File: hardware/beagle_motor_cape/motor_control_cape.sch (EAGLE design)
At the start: 26 parts, among them IC1 MCP4911SN, IC2 MCP4911SN

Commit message: Continue work on BeagleBone Black cape
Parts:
- removed IC3: (no value), INA219:INA219-SO8D
- added C4, C5, C6: 0.1uF, resistor:C-USC0603
- added D1, D2, D3, D4: 3.3V, diode:ZENER-DIODESOT23
- added LED1, LED2: (no value), adafruit:LEDCHIPLED_0603
- added Q7, Q8: (no value), adafruit:MOSFET-NREFLOW
- added R14, R15: 1k, rcl:R-US_R0603
- added R16, R18: 2k, rcl:R-US_R0603
- added R17: 11.3k, rcl:R-US_R0603
- added U1, U2: BTS50055-1TMA, BTS50055-1TMA:BTS50055-1TMA
- C3: value 1uF -> 0.1uF
- R10: value DNP -> 0
- R11: value DNP -> 681
- R12: value 4.7k -> 1k
- R13: value 4.7k -> 11.3k
- R7: value CSS2H-2512R-1L00F -> 681; device resistor:R-US_R6332 -> rcl:R-US_R0603
- R8: value 1k -> 0
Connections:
- net MOTOR0_SENSE renamed MOTOR0_TACH
- net MOTOR1_SENSE renamed MOTOR1_TACH
- removed net BATT0_IN: IC3.VIN+, R7.2
- removed net BATT0_OUT: IC3.VIN-, R7.1
- removed net I2C_SCL: IC3.SCL, R13.1
- removed net I2C_SDA: IC3.SDA, R12.1
- new net MOTOR0_EN: Q7.G, R14.2, R15.2
- new net MOTOR0_SENSE_AD: R10.2
- new net MOTOR1_EN: Q8.G, R12.2, R9.2
- new net MOTOR1_SENSE_AD: R8.2
- new net N$4: C4.1, D1.C, R10.1, R11.2, U1.IS
- new net N$5: Q7.D, U1.IN
- new net N$6: LED1.A, R15.1
- new net VCC: R13.2, U1.VBB@1, U1.VBB@2
- new net VCC_SENSE_AD: C5.1, D3.C, R13.1, R16.1
- new net VDD: R17.2, U2.VBB@1, U2.VBB@2
- new net VDD_SENSE_AD: C6.1, D4.C, R17.1, R18.1
- net +3V3: no longer R12.2, R13.2, R8.2, R9.2
- net GND: now also C4.2, C5.2, C6.2, D1.A, D2.A, D3.A, D4.A, LED1.C, LED2.C, Q7.S, Q8.S, R14.1, R16.2, R18.2, R7.1, R9.1, U1.OUT1, U1.OUT2, U1.OUT3, U1.OUT4, U2.OUT1, U2.OUT2, U2.OUT3, U2.OUT4; no longer R10.1
- net N$1: now also C3.1, D2.C, R7.2, R8.1, U2.IS; no longer IC3.A1, R10.2, R9.1
- net N$2: now also Q8.D, U2.IN; no longer IC3.A0, R11.2, R8.1
- net N$3: now also LED2.A, R12.1; no longer C3.1
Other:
- note added: "/FWD"
- note added: "/LDAC"
- note added: "/REV"
- note added: "1. Beaglebone Connector 2. Power Supply 3. Connectors 4. DAC and GPIO 5. High Side Switches"
- note added: "20V"
- note added: "3.3V Analog"
- note added: "ANA_X"
- note added: "BATT+"
- note added: "BATT-"
- note added: "BEAGLEBONE"
- note added: "CS"
- note added: "Connectors"
- note added: "DAC"
- note added: "ENABLE"
- note added: "FWD"
- note added: "GND"
- note added: "GPIO"
- note added: "GPIO_X"
- note added: "HS-Switch"
- note added: "High Side Switches"
- note added: "MOSI"
- note added: "MOTOR 0"
- note added: "MOTOR 1"
- note added: "OUT"
- note added: "PWM"
- note added: "Power Supply"
- note added: "REV"
- note added: "Ris sized to produce ~3V when IL = 60A"
- note added: "SCLK"
- note added: "SENSE"
- note added: "SPI0"
- note added: "SPI1"
- note added: "TACH"
- note added: "TRIGGER"
- note added: "VCC"
- note added: "VCC at 20V produces 3V on VCC_SENSE"
- note added: "VCC, VDD are independently supplied by one 1 battery pack each ~20V fully charged"
- note added: "VDD at 20V produces 3V on VDD_SENSE"
- note removed: "1. Beaglebone Connector 2. Power Suppply 3. DAC and GPIO"
- note removed: "Beaglebone Connector"
- note removed: "Current Sense"

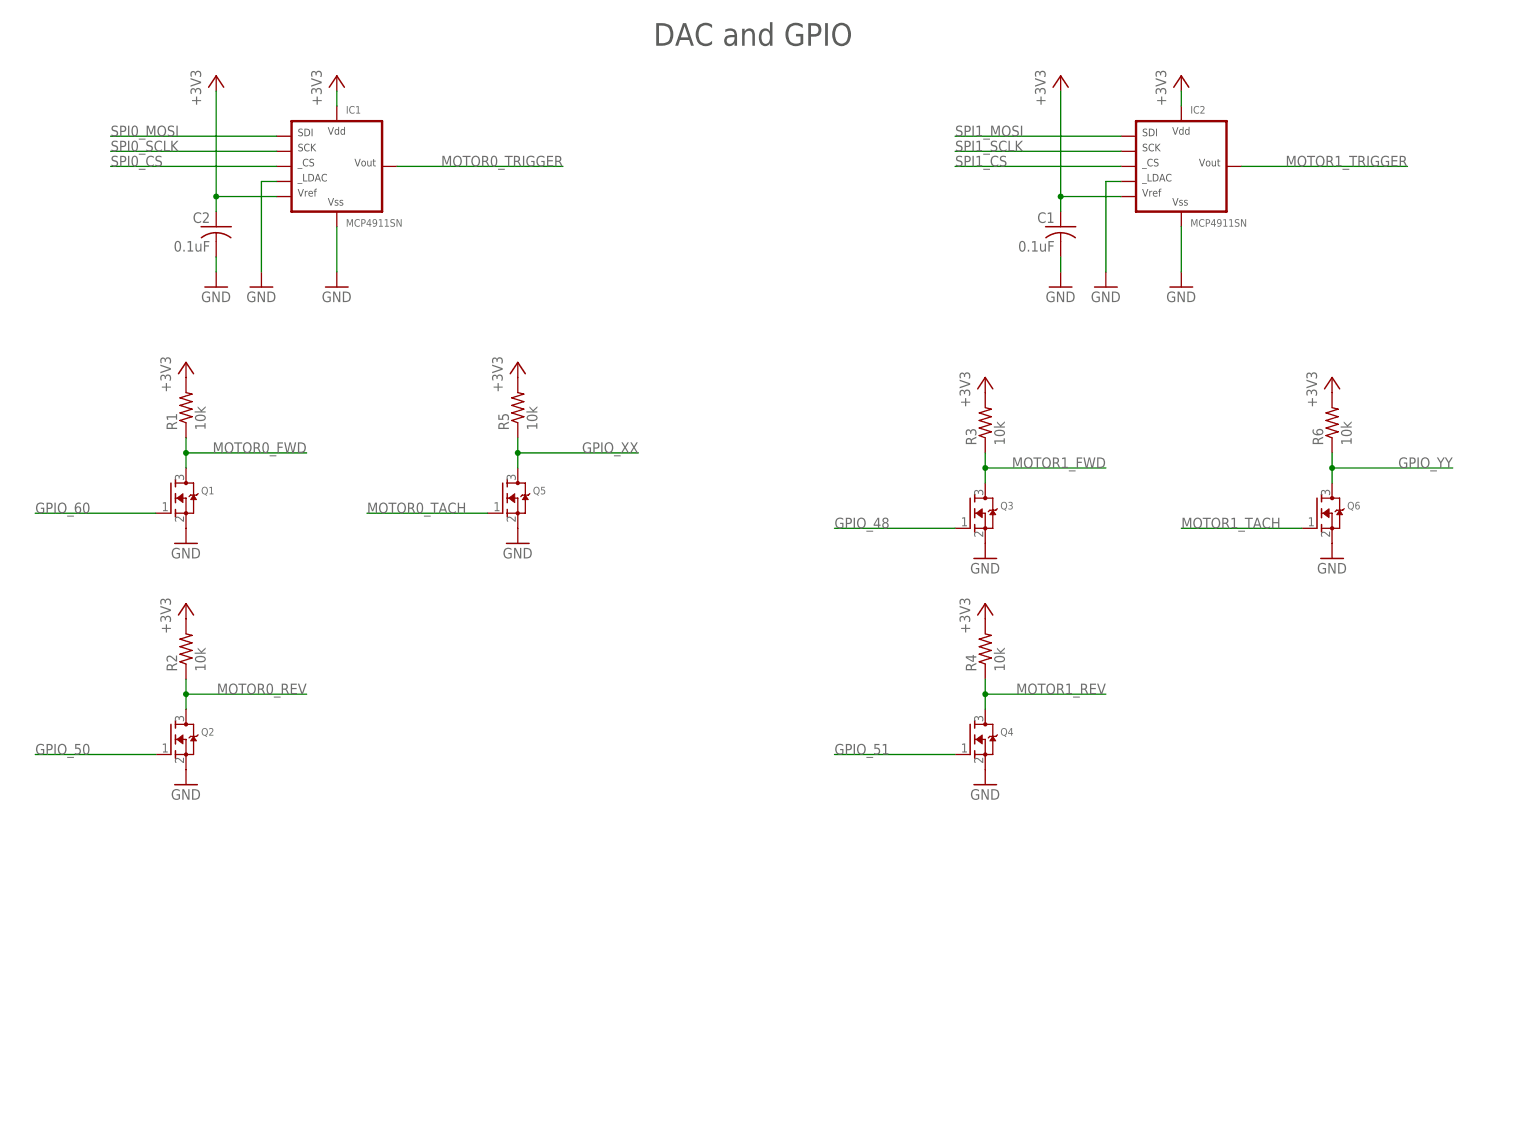
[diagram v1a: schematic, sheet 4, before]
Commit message: Finish motor control cape schematic
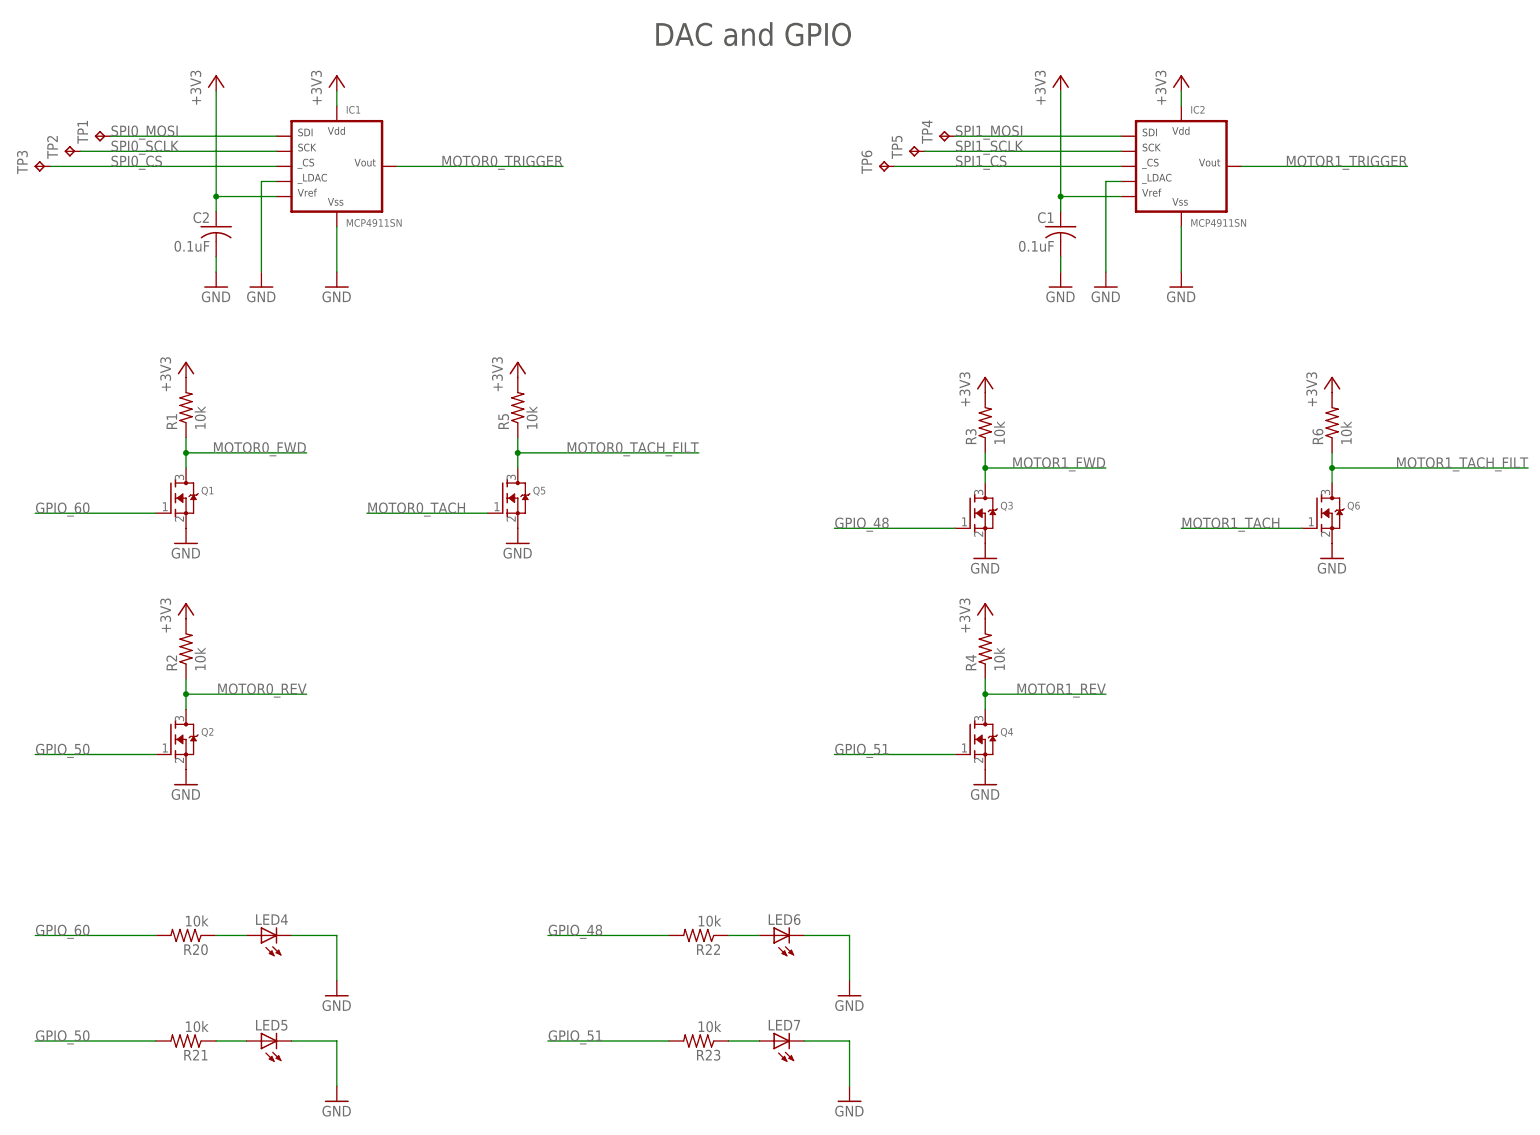
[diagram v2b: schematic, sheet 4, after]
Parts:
- added C7, C8: 4.7uF, resistor:C-USC0805
- added C9: 0.1uF, resistor:C-USC0603
- added D5: 1.8V, diode:ZENER-DIODESOT23
- added IC3: 7805TV, linear:7805TV
- added LED3, LED4, LED5, LED6, LED7: (no value), adafruit:LEDCHIPLED_0603
- added PAD1, PAD13, PAD14, PAD2, PAD3, PAD4: WIREPADSMD2,54-5,08, wirepad:WIREPADSMD2,54-5,08
- added PAD10, PAD11, PAD12, PAD5, PAD6, PAD7, PAD8, PAD9: WIREPAD2,54/1,0, wirepad:WIREPAD2,54/1,0
- added R19, R25: 1k, rcl:R-US_R0603
- added R20, R21, R22, R23: 10k, rcl:R-US_R0603
- added R24: 11.3k, rcl:R-US_R0603
- added TP1, TP2, TP3, TP4, TP5, TP6: TPB1,27, testpad:TPB1,27
- D1, D2, D3, D4: value 3.3V -> 1.8V
- R11, R7: value 681 -> 383
- R12, R15: value 1k -> 10k
- R16, R18: value 2k -> 1k
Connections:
- removed net GPIO_XX: Q5.D, R5.1
- removed net GPIO_YY: Q6.D, R6.1
- new net MOTOR0_HS: PAD2.P, U1.OUT1, U1.OUT2, U1.OUT3, U1.OUT4
- new net MOTOR0_TACH_FILT: Q5.D, R5.1, U$1.GPIO1_15
- new net MOTOR1_HS: PAD4.P, U2.OUT1, U2.OUT2, U2.OUT3, U2.OUT4
- new net MOTOR1_TACH_FILT: Q6.D, R6.1, U$1.GPIO1_14
- new net N$10: LED6.A, R22.1
- new net N$11: LED7.A, R23.1
- new net N$7: LED3.A, R19.1
- new net N$8: LED4.A, R20.1
- new net N$9: LED5.A, R21.1
- new net VBATT: C7.1, IC3.VI, PAD13.P, R24.2
- new net VBATT_SENSE_AD: C9.1, D5.C, R24.1, R25.1, U$1.AIN4
- net +3V3: now also U$1.VDD_3V3EXP@1, U$1.VDD_3V3EXP@2
- net +5V: now also C8.1, IC3.VO, R19.2, U$1.VDD_5V@1, U$1.VDD_5V@2; no longer U$1.SYS_5V@1, U$1.SYS_5V@2
- net GND: now also C7.2, C8.2, C9.2, D5.A, IC3.GND, LED3.C, LED4.C, LED5.C, LED6.C, LED7.C, PAD14.P, R25.2; no longer U1.OUT1, U1.OUT2, U1.OUT3, U1.OUT4, U2.OUT1, U2.OUT2, U2.OUT3, U2.OUT4
- net GPIO_48: now also R22.2
- net GPIO_50: now also R21.2
- net GPIO_51: now also R23.2
- net GPIO_60: now also R20.2
- net MOTOR0_FWD: now also PAD6.P
- net MOTOR0_REV: now also PAD7.P
- net MOTOR0_SENSE_AD: now also U$1.AIN1
- net MOTOR0_TACH: now also PAD12.P
- net MOTOR0_TRIGGER: now also PAD5.P
- net MOTOR1_FWD: now also PAD9.P
- net MOTOR1_REV: now also PAD10.P
- net MOTOR1_SENSE_AD: now also U$1.AIN3
- net MOTOR1_TACH: now also PAD11.P
- net MOTOR1_TRIGGER: now also PAD8.P
- net SPI0_CS: now also TP3.TP
- net SPI0_MOSI: now also TP1.TP
- net SPI0_SCLK: now also TP2.TP
- net SPI1_CS: now also TP6.TP
- net SPI1_MOSI: now also TP4.TP
- net SPI1_SCLK: now also TP5.TP
- net VCC: now also PAD1.P
- net VCC_SENSE_AD: now also U$1.AIN0
- net VDD: now also PAD3.P
- net VDD_SENSE_AD: now also U$1.AIN2
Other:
- note added: "Be lazy and use a Recom Power R-78E5.0-1.0"
- note added: "Ris sized to produce ~1.7V when IL = 60A"
- note added: "VBATT at 14V produces 1.15V on VBATT_SENSE"
- note added: "VCC at 20V produces 1.62V on VCC_SENSE"
- note added: "VDD at 20V produces 1.62V on VDD_SENSE"
- note removed: "Ris sized to produce ~3V when IL = 60A"
- note removed: "VCC at 20V produces 3V on VCC_SENSE"
- note removed: "VDD at 20V produces 3V on VDD_SENSE"

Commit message: More layout on motor control cape
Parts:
- removed R10, R8: 0, rcl:R-US_R0603
- removed TP1, TP2, TP3, TP4, TP5, TP6: TPB1,27, testpad:TPB1,27
- added D7: BAT60J, diode:BAT60J
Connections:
- removed net N$1: C3.1, D2.C, R7.2, R8.1, U2.IS
- removed net N$4: C4.1, D1.C, R10.1, R11.2, U1.IS
- new net VBATT_FILT: C7.1, D7.C, IC3.VI, R24.2
- net MOTOR0_EN: now also U$1.GPIO0_7
- net MOTOR0_SENSE_AD: now also C4.1, D1.C, R11.2, U1.IS; no longer R10.2
- net MOTOR1_EN: now also U$1.CLKOUT2
- net MOTOR1_SENSE_AD: now also C3.1, D2.C, R7.2, U2.IS; no longer R8.2
- net SPI0_CS: no longer TP3.TP
- net SPI0_MOSI: no longer TP1.TP
- net SPI0_SCLK: no longer TP2.TP
- net SPI1_CS: no longer TP6.TP
- net SPI1_MOSI: no longer TP4.TP
- net SPI1_SCLK: no longer TP5.TP
- net VBATT: now also D7.A; no longer C7.1, IC3.VI, R24.2

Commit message: Finish laying out motor control cape
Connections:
- new net N$1: U1.VBB@1
- net VCC: no longer U1.VBB@1
- net VCC_SENSE_AD: now also U$1.AIN2; no longer U$1.AIN0
- net VDD: no longer U2.VBB@1
- net VDD_SENSE_AD: now also U$1.AIN0; no longer U$1.AIN2
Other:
- note added: "Pin 8 is the tab"
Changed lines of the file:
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@@
 <net name="VCC_SENSE_AD" class="0">
-<segment>
-<pinref part="U$1" gate="G$1" pin="AIN0"/>
-<wire x1="114.3" y1="71.12" x2="63.5" y2="71.12" width="0.1524" layer="91"/>
-<label x="63.5" y="71.12" size="1.778" layer="95"/>
-</segment>
-</net>
-<net name="VDD_SENSE_AD" class="0">
 <segment>
 <pinref part="U$1" gate="G$1" pin="AIN2"/>
@@
 <wire x1="170.18" y1="68.58" x2="220.98" y2="68.58" width="0.1524" layer="91"/>
 <label x="220.98" y="68.58" size="1.778" layer="95" rot="MR0"/>
+</segment>
+</net>
+<net name="VDD_SENSE_AD" class="0">
+<segment>
+<pinref part="U$1" gate="G$1" pin="AIN0"/>
+<wire x1="114.3" y1="71.12" x2="63.5" y2="71.12" width="0.1524" layer="91"/>
+<label x="63.5" y="71.12" size="1.778" layer="95"/>
 </segment>
 </net>
@@
 <text x="50.8" y="78.74" size="1.778" layer="97">VCC at 20V produces 1.62V on VCC_SENSE</text>
 <text x="175.26" y="78.74" size="1.778" layer="97">VDD at 20V produces 1.62V on VDD_SENSE</text>
+<text x="129.54" y="147.32" size="1.778" layer="97">Pin 8 is the tab</text>
+<text x="248.92" y="144.78" size="1.778" layer="97">Pin 8 is the tab</text>
 </plain>
 <instances>
@@
 <pinref part="SUPPLY2" gate="G$1" pin="VCC"/>
 <wire x1="121.92" y1="147.32" x2="124.46" y2="147.32" width="0.1524" layer="91"/>
-<wire x1="124.46" y1="147.32" x2="124.46" y2="149.86" width="0.1524" layer="91"/>
-<pinref part="U1" gate="G$1" pin="VBB@1"/>
-<wire x1="124.46" y1="149.86" x2="124.46" y2="162.56" width="0.1524" layer="91"/>
-<wire x1="121.92" y1="149.86" x2="124.46" y2="149.86" width="0.1524" layer="91"/>
-<junction x="124.46" y="149.86"/>
+<wire x1="124.46" y1="147.32" x2="124.46" y2="162.56" width="0.1524" layer="91"/>
 </segment>
 <segment>
@@
 <pinref part="U2" gate="G$1" pin="VBB@2"/>
 <wire x1="243.84" y1="144.78" x2="246.38" y2="144.78" width="0.1524" layer="91"/>
-<wire x1="246.38" y1="144.78" x2="246.38" y2="147.32" width="0.1524" layer="91"/>
-<pinref part="U2" gate="G$1" pin="VBB@1"/>
-<wire x1="246.38" y1="147.32" x2="246.38" y2="157.48" width="0.1524" layer="91"/>
-<wire x1="243.84" y1="147.32" x2="246.38" y2="147.32" width="0.1524" layer="91"/>
-<junction x="246.38" y="147.32"/>
+<wire x1="246.38" y1="144.78" x2="246.38" y2="157.48" width="0.1524" layer="91"/>
 <pinref part="SUPPLY1" gate="G$1" pin="VDD"/>
 </segment>
@@
 </segment>
 </net>
+<net name="N$1" class="0">
+<segment>
+<pinref part="U1" gate="G$1" pin="VBB@1"/>
+<wire x1="121.92" y1="149.86" x2="119.38" y2="149.86" width="0.1524" layer="91"/>
+</segment>
+</net>
